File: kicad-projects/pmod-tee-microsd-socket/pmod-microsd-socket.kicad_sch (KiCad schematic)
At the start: 5 parts, among them J1 PMOD_Host_Conn_02x06, J2 Detect Switch, J3 Micro_SD_Card_Det2

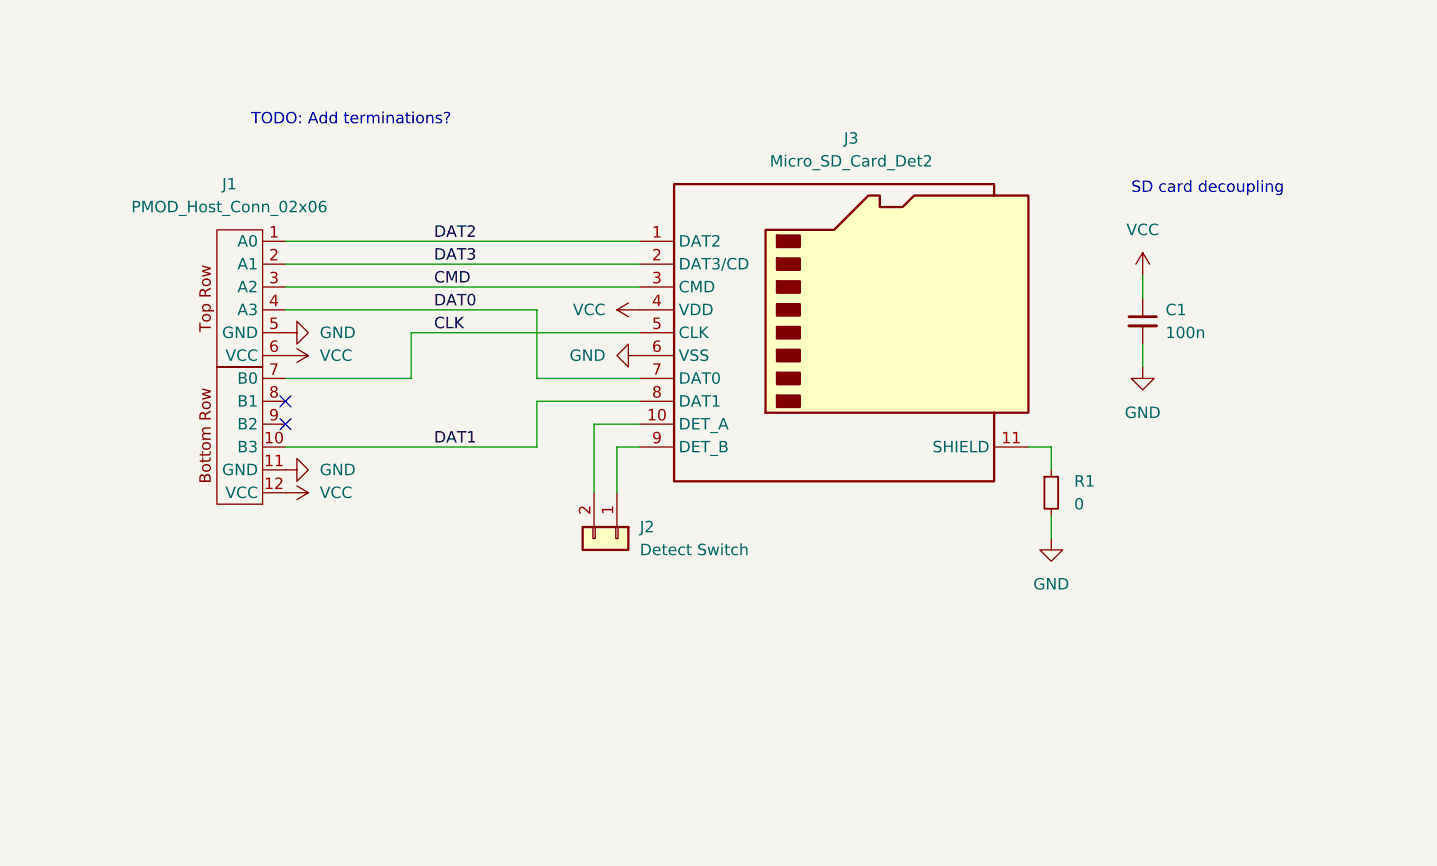
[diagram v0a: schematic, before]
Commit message: Add another PMOD connector to schem. Lay out PCB
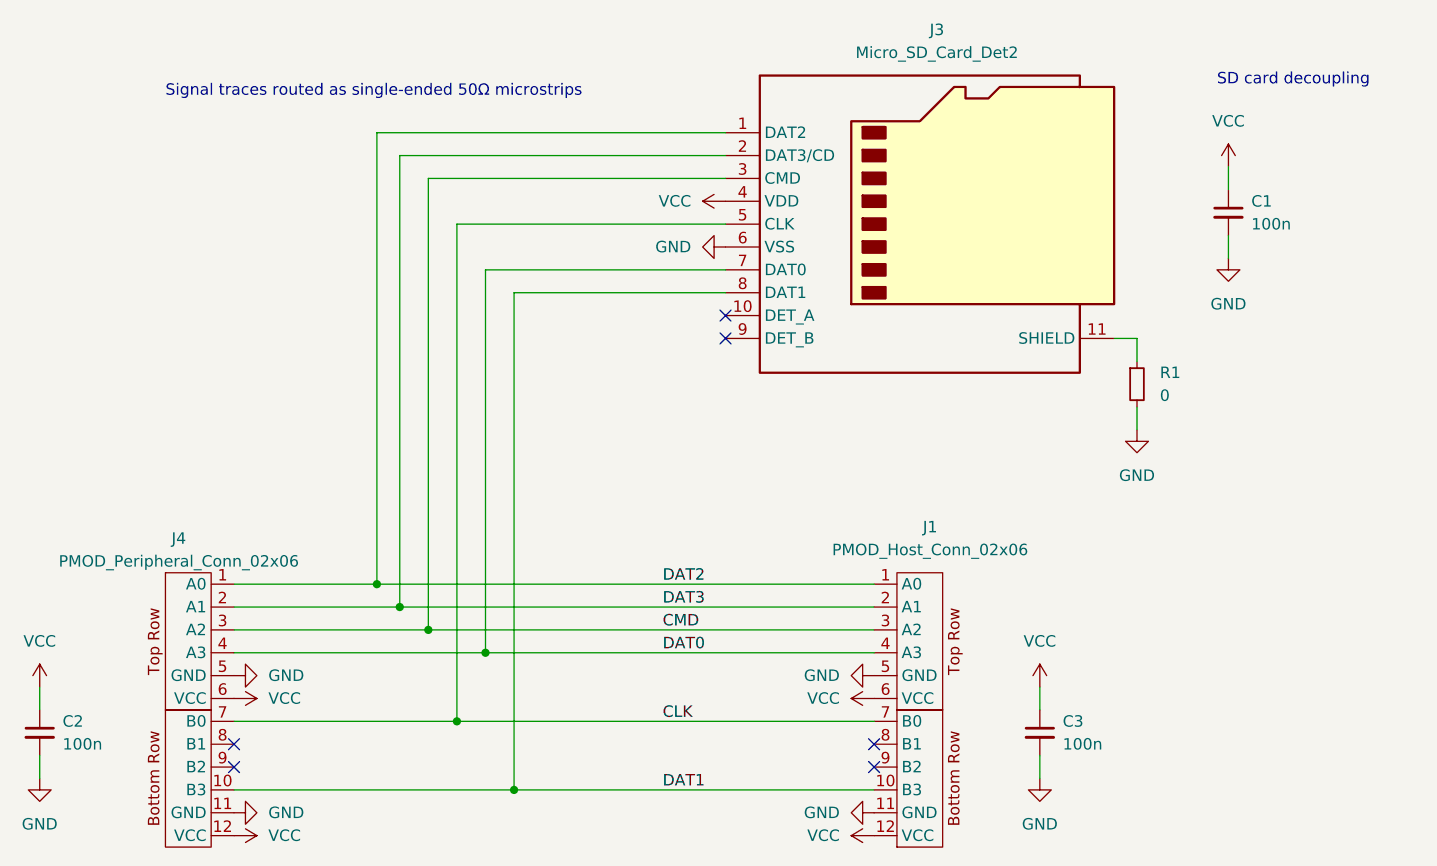
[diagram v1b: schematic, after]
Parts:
- removed J2: Detect Switch, Connector_PinHeader_2.54mm:PinHeader_1x02_P2.54mm_Vertical, symbol Connector_Generic:Conn_01x02
- added C2, C3: 100n, Capacitor_SMD:C_0603_1608Metric, symbol Device:C_Small
- added J4: PMOD_Peripheral_Conn_02x06, pmod:PMOD_PinHeader_2x06_P2.54mm_Horizontal, symbol pmod:PMOD_Peripheral_Conn_02x06
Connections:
- net CLK: now also J4.7 (B0)
- net CMD: now also J4.3 (A2)
- net DAT0: now also J4.4 (A3)
- net DAT1: now also J4.10 (B3)
- net DAT2: now also J4.1 (A0)
- net DAT3: now also J4.2 (A1)
- net GND: now also C2.2, C3.2, J4.11 (GND), J4.5 (GND)
- net VCC: now also C2.1, C3.1, J4.12 (VCC), J4.6 (VCC)
- no-connect marks 2 -> 6
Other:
- note added: "Signal traces routed as single-ended 50Ω microstrips"
- note removed: "TODO: Add terminations?"
- moved on the sheet: C1, J1, J3, R1
